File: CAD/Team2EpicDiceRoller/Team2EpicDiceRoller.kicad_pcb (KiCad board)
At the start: 2 copper layers, 45 parts, among them J1 Conn_02x03_Odd_Even, J2 Conn_01x16, J3 Conn_01x02_9VBatt, Q1 BS170, Q2 2N2222, SW3 RotaryEncoder_Switch, SW5 SW_LeftMenu, SW6 SW_MidMenu, SW7 SW_Reset, SW8 SW_RightMenu, U1 74HC14, U2 ATmega328P-P, Y1 Crystal_16MHz

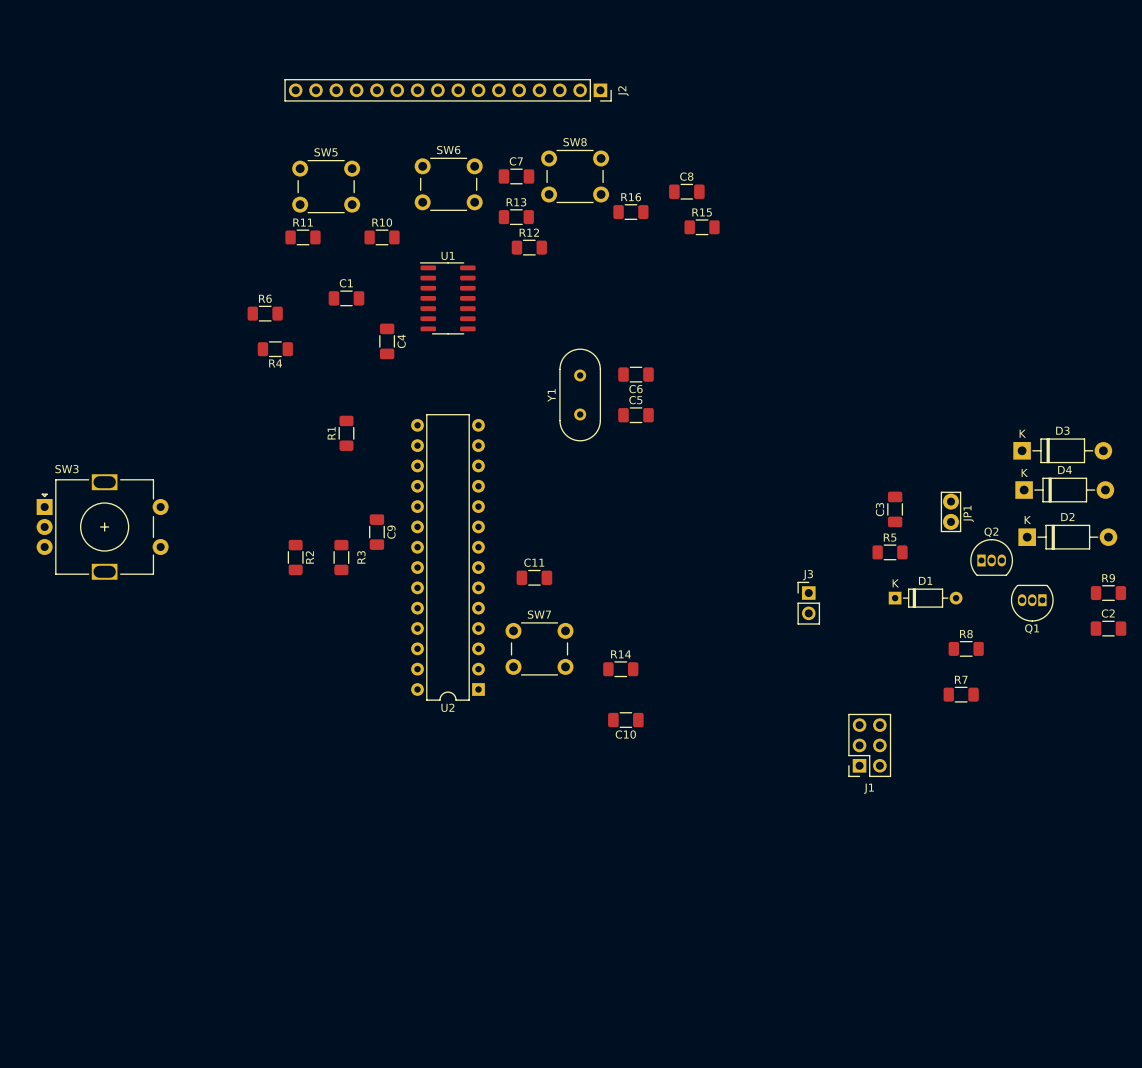
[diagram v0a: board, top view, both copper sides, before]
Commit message: Initial routing - done poorly, need to update power switch footprint
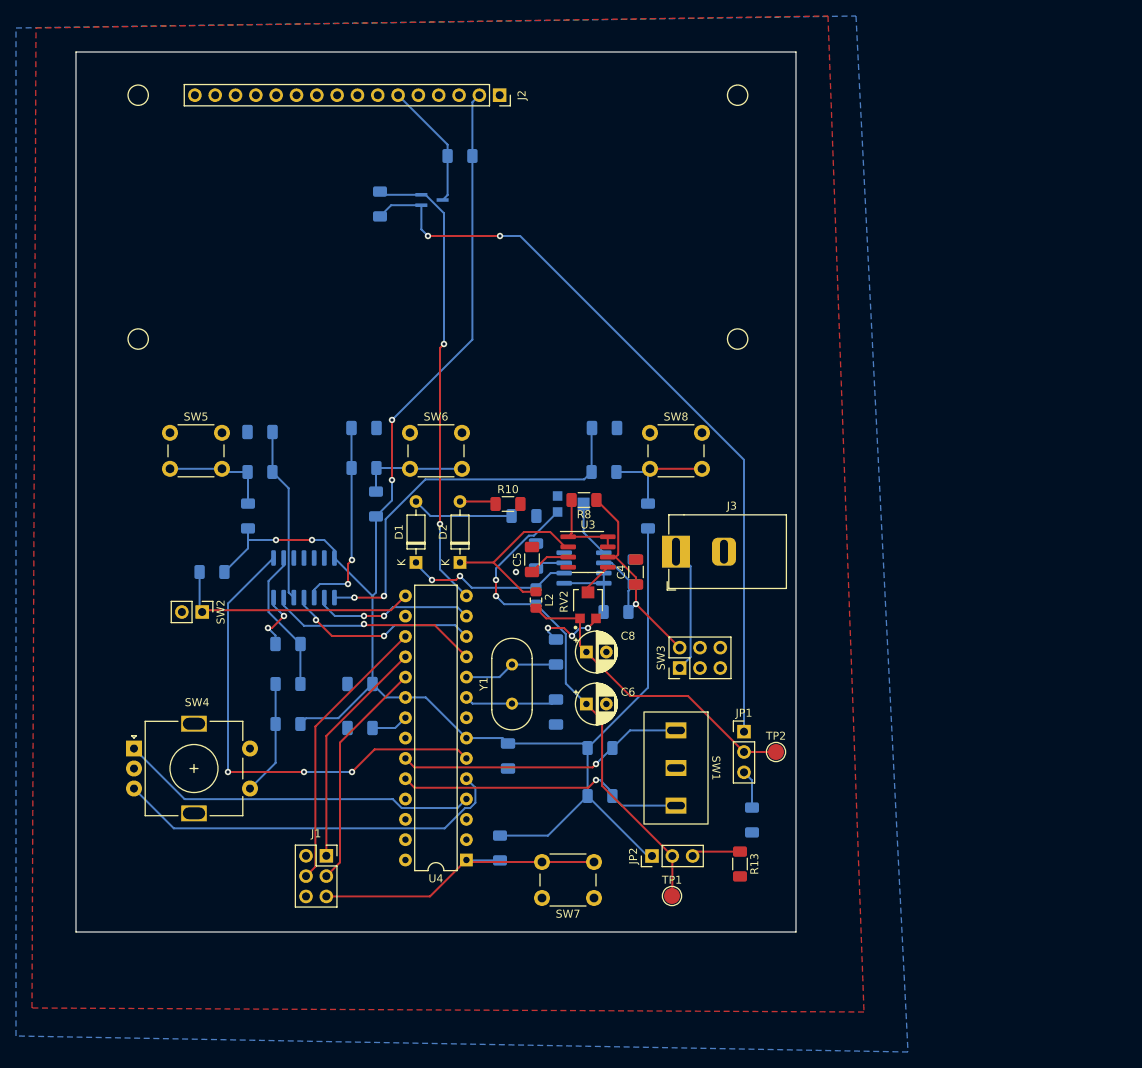
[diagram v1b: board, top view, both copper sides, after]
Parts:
- removed D3, D4: 1N4007, Diode_THT:D_DO-41_SOD81_P10.16mm_Horizontal
- removed Q2: 2N2222, Package_TO_SOT_THT:TO-92_Inline
- added C12: 10u, Capacitor_SMD:C_1206_3216Metric_Pad1.33x1.80mm_HandSolder, B.Cu at (163.1, 67.0)
- added C13: 100n, Capacitor_SMD:C_1206_3216Metric_Pad1.33x1.80mm_HandSolder, B.Cu at (132.5, 104.5)
- added C14: 100n, Capacitor_SMD:C_1206_3216Metric_Pad1.33x1.80mm_HandSolder, B.Cu at (151.0, 108.0)
- added C15: 100n, Capacitor_SMD:C_1206_3216Metric_Pad1.33x1.80mm_HandSolder, B.Cu at (132.5, 99.0)
- added JP2: Jumper_3_Open, Connector_PinHeader_2.54mm:PinHeader_1x03_P2.54mm_Vertical, F.Cu at (169.0, 120.5)
- added L1: 100u, Inductor_SMD:L_0805_2012Metric_Pad1.15x1.40mm_HandSolder, B.Cu at (154.5, 88.0)
- added L2: 100u, Inductor_SMD:L_0805_2012Metric_Pad1.15x1.40mm_HandSolder, F.Cu at (154.5, 88.5)
- added R17: 1k, Resistor_SMD:R_1206_3216Metric_Pad1.30x1.75mm_HandSolder, B.Cu at (133.0, 72.0)
- added R18: 10k, Resistor_SMD:R_1206_3216Metric_Pad1.30x1.75mm_HandSolder, B.Cu at (150.0, 119.5)
- added R19: 1k, Resistor_SMD:R_1206_3216Metric_Pad1.30x1.75mm_HandSolder, B.Cu at (168.5, 78.0)
- added R20: 1k, Resistor_SMD:R_1206_3216Metric_Pad1.30x1.75mm_HandSolder, B.Cu at (163.0, 72.5)
- added RV1: 5k, Library:TRIM_TC33X-2-502E, B.Cu at (159.0, 76.5)
- added RV2: 5k, Library:TRIM_TC33X-2-502E, F.Cu at (161.0, 89.0)
- added SW1: SW_Toggle_SPDT, Library:GoldSun_MTS103_Mini_Toggle_Switch, F.Cu at (172.0, 109.5)
- added SW2: Tilt_Switch, Connector_PinHeader_2.54mm:PinHeader_1x02_P2.54mm_Vertical, F.Cu at (112.8, 90.0)
- added SW4: RotaryEncoder_Switch, Rotary_Encoder:RotaryEncoder_Alps_EC11E-Switch_Vertical_H20mm, F.Cu at (104.2, 107.1)
- added TP1: TestPoint, TestPoint:TestPoint_Pad_D2.0mm, F.Cu at (171.5, 125.5)
- added TP2: TestPoint, TestPoint:TestPoint_Pad_D2.0mm, F.Cu at (184.5, 107.5)
- added U3: MC34063AD, Package_SO:SOIC-8_3.9x4.9mm_P1.27mm, F.Cu at (161.0, 82.5)
- added U4: ATmega328P-P, Package_DIP:DIP-28_W7.62mm, F.Cu at (145.8, 121.0)
- C1: value 10u -> 100u; moved to B.Cu
- C10, C9: value 100n -> 30p; moved to B.Cu
- C11: value 100n -> 10u; moved to B.Cu
- C2: value 1u -> 470p; moved to B.Cu
- C3: value 10p -> 10u; moved to B.Cu
- C4: value 10u -> 100u
- C5: value 30p -> 470p
- C6: value 30p -> 470u; footprint Capacitor_SMD:C_1206_3216Metric_Pad1.33x1.80mm_HandSolder -> Capacitor_THT:CP_Radial_D5.0mm_P2.50mm
- C7, R1, R11, R14, R15, R2, R3, R4, R6: moved to B.Cu
- C8: value 10u -> 470u; footprint Capacitor_SMD:C_1206_3216Metric_Pad1.33x1.80mm_HandSolder -> Capacitor_THT:CP_Radial_D5.0mm_P2.50mm
- D1: value BZX55C3V0 -> BZX55C5V1
- D2: value 1N4007 -> BZX55C3V9; footprint Diode_THT:D_DO-41_SOD81_P10.16mm_Horizontal -> Diode_THT:D_DO-35_SOD27_P7.62mm_Horizontal
- J3: value Conn_01x02_9VBatt -> Barrel_Jack; footprint Connector_PinHeader_2.54mm:PinHeader_1x02_P2.54mm_Vertical -> Library:BarrelJack_CUI_PJ-037A_Horizontal
- JP1: value Jumper_2_Bridged -> Jumper_3_Open; footprint TestPoint:TestPoint_Bridge_Pitch2.54mm_Drill1.0mm -> Connector_PinHeader_2.54mm:PinHeader_1x03_P2.54mm_Vertical
- Q1: value BS170 -> BSS138; footprint Package_TO_SOT_THT:TO-92_Inline -> Package_TO_SOT_SMD:SOT-323_SC-70_Handsoldering; moved to B.Cu
- R10: value 1k -> 120
- R12: value 1k -> 150; moved to B.Cu
- R13: value 1k -> 150
- R16: value 1k -> 10k; moved to B.Cu
- R5: value 2Meg -> 0.33; moved to B.Cu
- R7: value 2Meg -> 68; moved to B.Cu
- R8: value 500k -> 0.33
- R9: value 10K -> 1k; moved to B.Cu
- SW3: value RotaryEncoder_Switch -> SW_Power; footprint Rotary_Encoder:RotaryEncoder_Alps_EC11E-Switch_Vertical_H20mm -> Connector_PinHeader_2.54mm:PinHeader_2x03_P2.54mm_Vertical
- U1: value 74HC14 -> MC34063AD; footprint Package_SO:SOIC-14_3.9x8.7mm_P1.27mm -> Package_SO:SOIC-8_3.9x4.9mm_P1.27mm; moved to B.Cu
- U2: value ATmega328P-P -> 74HC14; footprint Package_DIP:DIP-28_W7.62mm -> Package_SO:SOIC-14_3.9x8.7mm_P1.27mm; moved to B.Cu
- moved R9 108.0 mm to (118.5, 78.0), turned to 90 degrees
- moved Q1 91.2 mm to (141.5, 38.5), turned to 0 degrees
- moved R13 85.6 mm to (180.0, 121.5), turned to -90 degrees
- moved SW3 81.9 mm to (172.5, 97.0), turned to 90 degrees
- moved C3 77.7 mm to (123.5, 94.0), turned to 180 degrees
- moved R12 76.8 mm to (181.5, 116.0), turned to -90 degrees
- moved C2 72.1 mm to (154.5, 83.0), turned to 90 degrees
- moved D2 71.0 mm to (145.0, 83.8), turned to 90 degrees
- moved J1 67.6 mm to (128.3, 120.5), turned to 0 degrees
- moved R14 65.5 mm to (135.0, 39.0), turned to 90 degrees
- moved D1 60.1 mm to (139.5, 83.8), turned to 90 degrees
- moved R7 59.0 mm to (153.0, 78.0)
- moved C8 58.9 mm to (160.8, 95.0)
- moved R15 53.5 mm to (134.5, 76.5), turned to 90 degrees
- moved R8 51.3 mm to (160.5, 76.0), turned to 180 degrees
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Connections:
- C1 pad 1: Net-(R6-Pad2) -> /Vin
- C10 pad 2: VCC -> Net-(C10-Pad2)
- C11 pad 1: GND -> /MidDebn
- C11 pad 2: VCC -> GND
- C2 pad 1: Net-(D4-Pad2) -> Net-(C2-Pad1)
- C3 pad 1: Net-(D2-Pad1) -> /EncDebnc
- C4 pad 1: Net-(R11-Pad2) -> /Vin
- C5 pad 1: GND -> Net-(C5-Pad1)
- C5 pad 2: Net-(U2-Pad9) -> GND
- C6 pad 1: GND -> Net-(C6-Pad1)
- C6 pad 2: Net-(U2-Pad10) -> GND
- C7 pad 1: Net-(R13-Pad2) -> /LeftDebn
- C8 pad 1: Net-(R16-Pad2) -> Net-(C8-Pad1)
- J1 pad 2: ICSP_5V -> unconnected-(J1-Pad2)
- J2 pad 6: IO8_PB0 -> LCD_RX
- JP1 pad 1: Net-(D2-Pad1) -> +3V3
- Q1 pad 1: Net-(D2-Pad2) -> +3V3
- Q1 pad 2: Net-(Q1-Pad2) -> IO8_PB0
- Q1 pad 3: Net-(D1-Pad2) -> LCD_RX
- R10 pad 1: VCC -> Net-(D2-Pad2)
- R10 pad 2: Net-(R10-Pad2) -> GND
- R11 pad 1: Net-(R10-Pad2) -> Net-(R11-Pad1)
- R11 pad 2: Net-(R11-Pad2) -> /LeftDebn
- R12 pad 1: VCC -> Net-(JP1-Pad3)
- R12 pad 2: Net-(R12-Pad2) -> GND
- R13 pad 1: Net-(R12-Pad2) -> Net-(JP2-Pad3)
- R13 pad 2: Net-(R13-Pad2) -> GND
- R14 pad 1: VCC -> +3V3
- R14 pad 2: RESET# -> IO8_PB0
- R16 pad 1: Net-(R15-Pad2) -> VCC
- R16 pad 2: Net-(R16-Pad2) -> LCD_RX
- R5 pad 1: Net-(D1-Pad1) -> /Vin
- R5 pad 2: Net-(Q1-Pad2) -> Net-(R5-Pad2)
- R6 pad 2: Net-(R6-Pad2) -> /EncDebnc
- R7 pad 1: ICSP_5V -> Net-(D1-Pad2)
- R7 pad 2: Net-(Q2-Pad2) -> GND
- R8 pad 1: Net-(Q2-Pad2) -> /Vin
- R8 pad 2: GND -> Net-(R8-Pad2)
- R9 pad 1: Net-(D2-Pad1) -> VCC
- R9 pad 2: Net-(D4-Pad2) -> Net-(R11-Pad1)
- SW5 pad 2: Net-(R10-Pad2) -> Net-(R11-Pad1)
- SW6 pad 2: Net-(R12-Pad2) -> Net-(R15-Pad2)
- SW8 pad 2: Net-(R15-Pad2) -> Net-(R19-Pad2)
- U1 pad 1: Net-(R6-Pad2) -> Net-(R5-Pad2)
- U1 pad 2: IO4_PD4 -> Net-(D1-Pad1)
- U1 pad 3: Net-(R11-Pad2) -> Net-(C2-Pad1)
- U1 pad 4: IO5_PD5 -> GND
- U1 pad 5: Net-(R13-Pad2) -> Net-(RV1-Pad2)
- U1 pad 6: IO6_PD6 -> /Vin
- U1 pad 7: GND -> Net-(R5-Pad2)
- U1 pad 8: IO7_PD7 -> Net-(R5-Pad2)
- U2 pad 1: RESET# -> /RigDebn
- U2 pad 10: Net-(U2-Pad10) -> unconnected-(U2-Pad10)
- U2 pad 11: IO5_PD5 -> GND
- U2 pad 12: IO6_PD6 -> unconnected-(U2-Pad12)
- U2 pad 13: IO7_PD7 -> GND
- U2 pad 14: IO8_PB0 -> VCC
- U2 pad 2: IO0_RX_PD0 -> IO7_PD7
- U2 pad 3: IO1_TX_PD1 -> /MidDebn
- U2 pad 4: IO2_PD2 -> IO6_PD6
- U2 pad 5: IO3_PD3 -> /LeftDebn
- U2 pad 6: IO4_PD4 -> IO5_PD5
- U2 pad 7: VCC -> GND
- U2 pad 8: GND -> IO4_PD4
- U2 pad 9: Net-(U2-Pad9) -> /EncDebnc
- Y1 pad 1: Net-(U2-Pad9) -> Net-(C9-Pad2)
- Y1 pad 2: Net-(U2-Pad10) -> Net-(C10-Pad2)
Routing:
- net VCC: track 0.00 -> 206.9 mm, vias 0 -> 4
- net +3V3: track 0.00 -> 95.0 mm, vias 0 -> 2
- net Net-(C6-Pad1): track 0.00 -> 63.0 mm, vias 0 -> 2
- net IO4_PD4: track 0.00 -> 60.5 mm, vias 0 -> 3
- net IO8_PB0: track 0.00 -> 58.5 mm, vias 0 -> 2
- net /RigDebn: track 0.00 -> 49.7 mm, vias 0 -> 2
- net IO3_PD3: track 0.00 -> 49.5 mm
- net IO2_PD2: track 0.00 -> 45.1 mm
- net RESET#: track 0.00 -> 39.7 mm
- net Net-(C8-Pad1): track 0.00 -> 39.4 mm
- net AD1_PC1: track 0.00 -> 36.3 mm, vias 0 -> 1
- net AD0_PC0: track 0.00 -> 36.2 mm, vias 0 -> 1
- net IO11_MOSI_PB3: track 0.00 -> 35.1 mm
- net /Vin: track 0.00 -> 34.2 mm, vias 0 -> 1
- net IO9_PB1: track 0.00 -> 31.4 mm
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- added copper zone on B.Cu, net GND
- added copper zone on F.Cu, net GND
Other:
- board outline added: 90 x 110 mm

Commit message: Updated schematic to remove traces and update the footprints
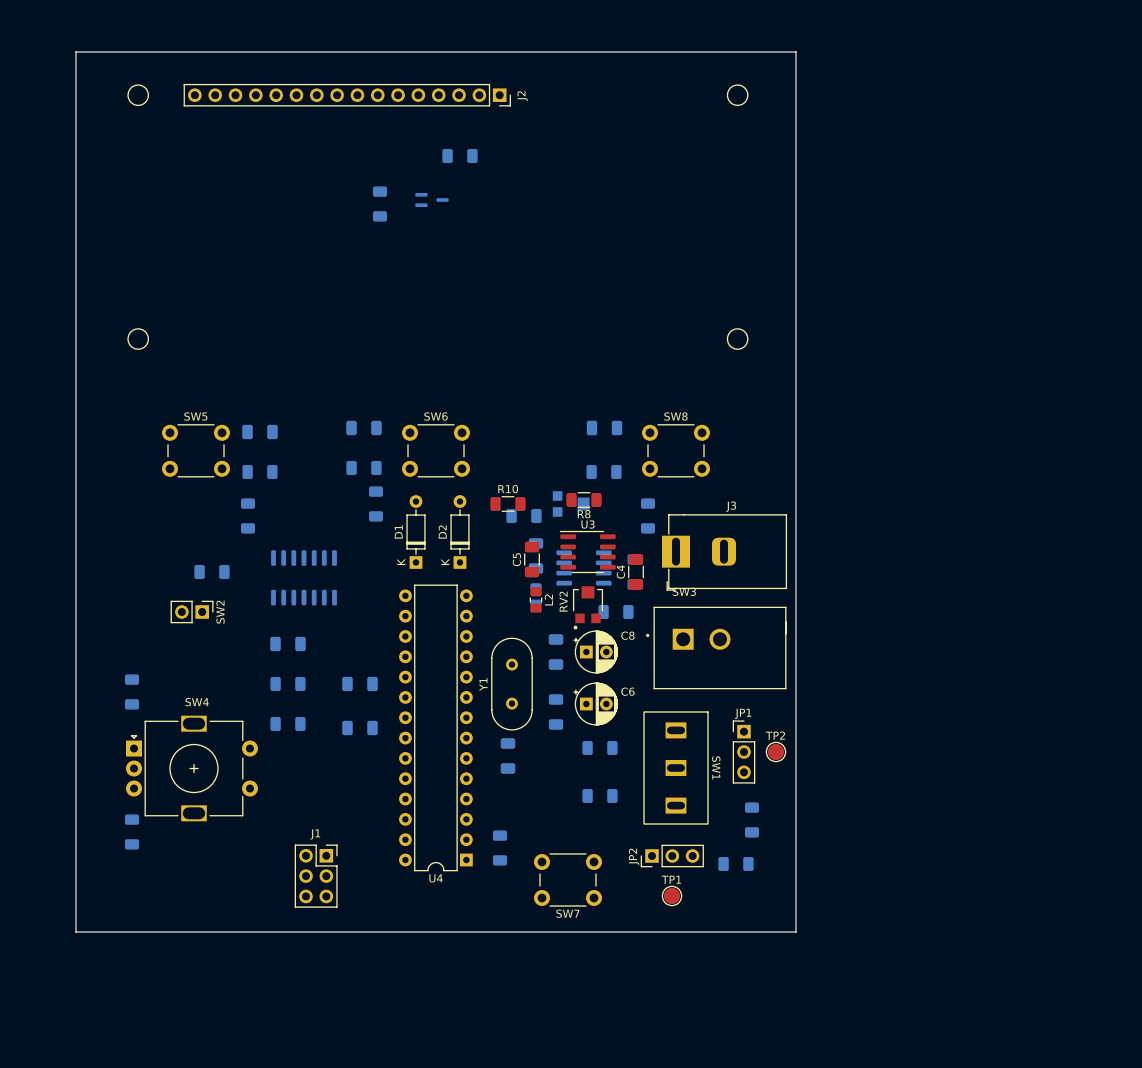
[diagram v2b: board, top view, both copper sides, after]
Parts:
- added R21: 5.1k, Resistor_SMD:R_1206_3216Metric_Pad1.30x1.75mm_HandSolder, B.Cu at (104.0, 100.0)
- added R22: 5.1k, Resistor_SMD:R_1206_3216Metric_Pad1.30x1.75mm_HandSolder, B.Cu at (104.0, 117.5)
- R13: moved to B.Cu
- SW3: footprint Connector_PinHeader_2.54mm:PinHeader_2x03_P2.54mm_Vertical -> GF-123-0054:SW_GF-123-0054
- moved SW3 5.63 mm to (177.5, 94.5), turned to 0 degrees
- moved R13 0.50 mm to (179.5, 121.5), turned to 0 degrees
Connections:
- SW4 pad A: IO2_PD2 -> Net-(R21-Pad1)
- SW4 pad B: IO3_PD3 -> Net-(R22-Pad2)
- SW4 pad MP: (no net) -> GND
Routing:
- net VCC: track 206.9 -> 0.00 mm, vias 4 -> 0
- net +3V3: track 95.0 -> 0.00 mm, vias 2 -> 0
- net Net-(C6-Pad1): track 63.0 -> 0.00 mm, vias 2 -> 0
- net IO4_PD4: track 60.5 -> 0.00 mm, vias 3 -> 0
- net IO8_PB0: track 58.5 -> 0.00 mm, vias 2 -> 0
- net /RigDebn: track 49.7 -> 0.00 mm, vias 2 -> 0
- net IO3_PD3: track 49.5 -> 0.00 mm
- net IO2_PD2: track 45.1 -> 0.00 mm
- net RESET#: track 39.7 -> 0.00 mm
- net Net-(C8-Pad1): track 39.4 -> 0.00 mm
- net AD1_PC1: track 36.3 -> 0.00 mm, vias 1 -> 0
- net AD0_PC0: track 36.2 -> 0.00 mm, vias 1 -> 0
- net IO11_MOSI_PB3: track 35.1 -> 0.00 mm
- net /Vin: track 34.2 -> 0.00 mm, vias 1 -> 0
- net IO9_PB1: track 31.4 -> 0.00 mm
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- removed copper zone on B.Cu, net GND
- removed copper zone on F.Cu, net GND

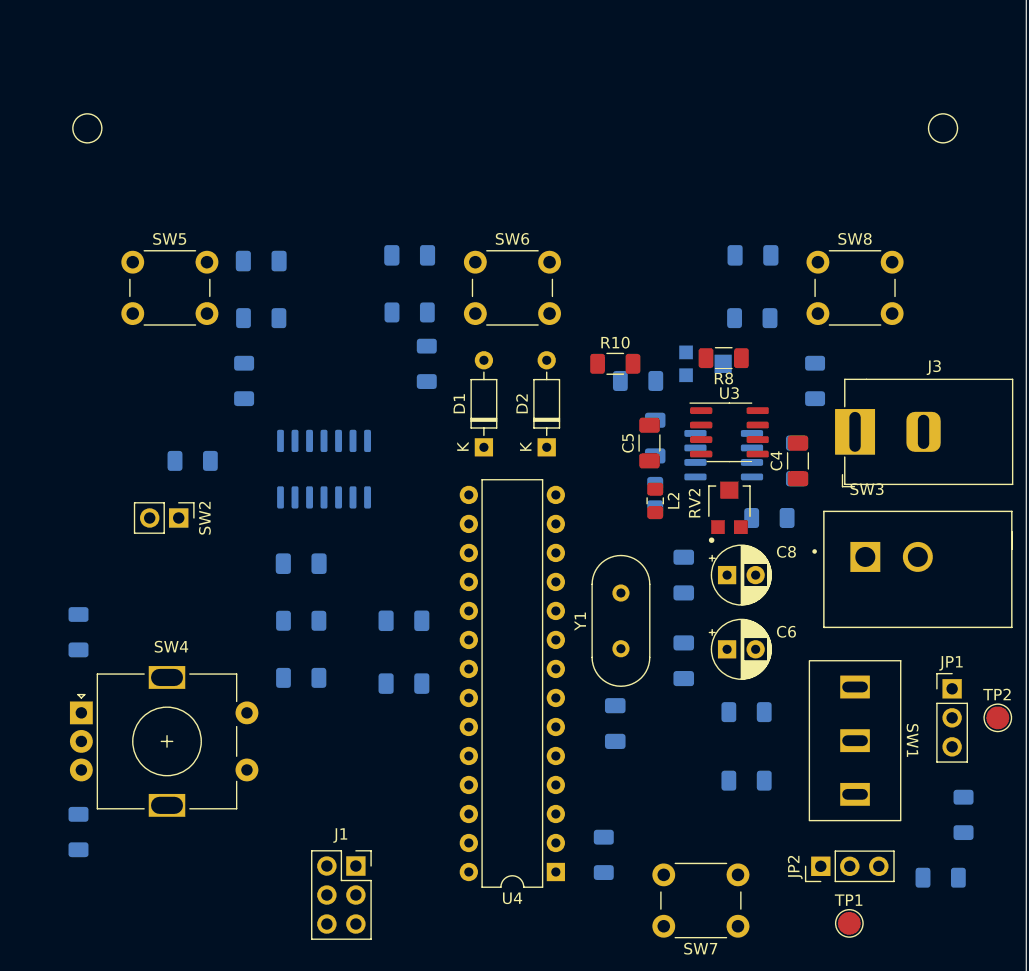
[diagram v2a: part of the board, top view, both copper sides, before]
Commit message: Added mounting holes for the standoffs
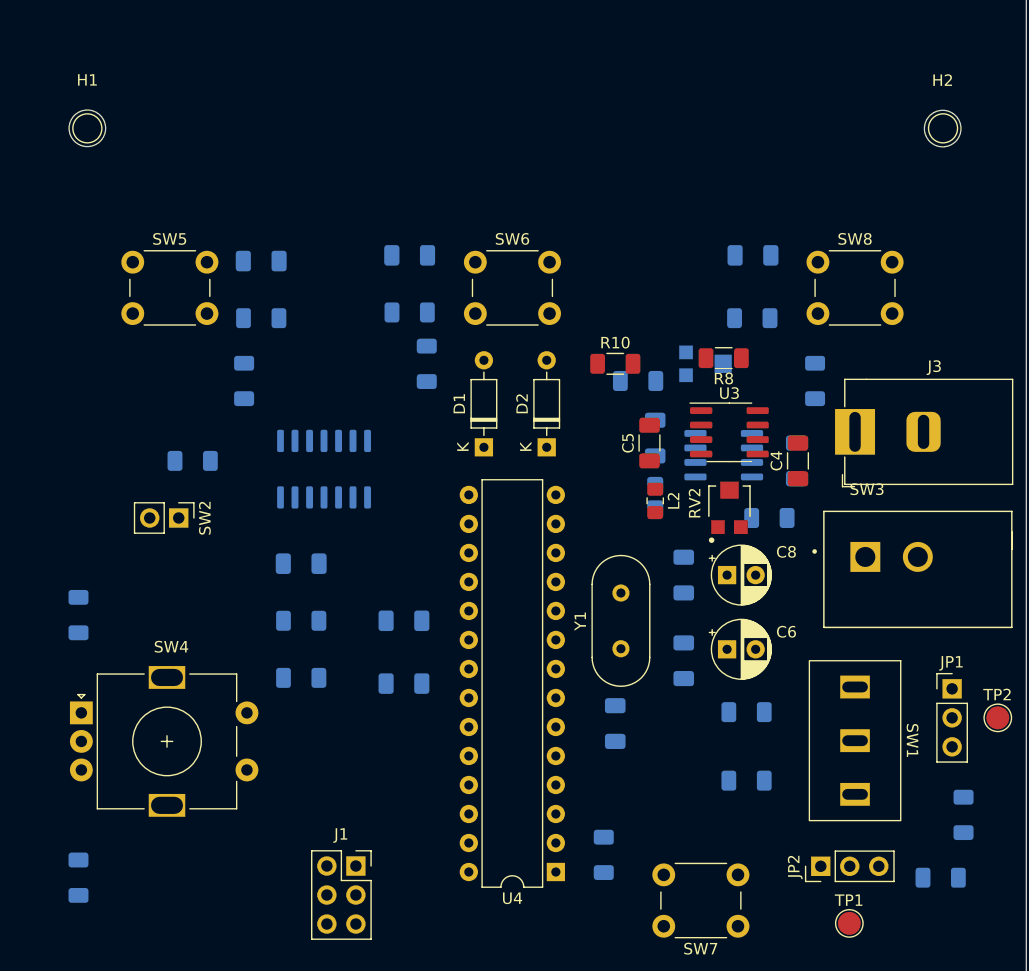
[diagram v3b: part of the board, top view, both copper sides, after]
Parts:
- added H1: MountingHole, MountingHole:MountingHole_3.2mm_M3, F.Cu at (104.8, 55.9)
- added H2: MountingHole, MountingHole:MountingHole_3.2mm_M3, F.Cu at (179.7, 55.9)
- J2: footprint Connector_PinSocket_2.54mm:PinSocket_1x16_P2.54mm_Vertical -> Library:PinSocket_1x16_P2.54mm_Vertical_LCD
- moved R22 4.00 mm to (104.0, 121.5)
- moved R21 1.50 mm to (104.0, 98.5)
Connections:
- net Net-(JP1-Pad3) renamed /Load_3V3
- net Net-(JP2-Pad3) renamed /Load_VCC
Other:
- rule pad_to_mask_clearance: 0 -> 0.0508

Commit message: Newer version
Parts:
- added TPG1: TestPointGND, TestPoint:TestPoint_Pad_D2.0mm, F.Cu at (168.7, 88.0)
- added TPG2: TestPointGND, TestPoint:TestPoint_Pad_D2.0mm, F.Cu at (101.1, 95.3)
- C1, C2, L1, R13, R5, R7, RV1, U1: moved to F.Cu
- TP1: value TestPoint -> TestPointVCC
- TP2: value TestPoint -> TestPoint3V3
- moved TP2 85.0 mm to (101.1, 90.7)
- moved R12 78.5 mm to (104.7, 99.6)
- moved JP1 77.6 mm to (104.8, 88.0)
- moved SW4 62.8 mm to (166.8, 113.2)
- moved R2 61.3 mm to (101.7, 120.8)
- moved R3 61.2 mm to (101.5, 111.5)
- moved SW1 60.7 mm to (111.6, 115.7)
- moved L2 59.7 mm to (110.2, 48.4)
- moved R21 57.2 mm to (159.8, 110.9), turned to 180 degrees
- moved R22 56.1 mm to (159.8, 116.0), turned to 0 degrees
- moved D2 54.9 mm to (112.0, 40.0), turned to 0 degrees
- moved U3 52.7 mm to (123.2, 45.8)
- moved C5 51.9 mm to (115.8, 48.4)
- moved C8 49.8 mm to (111.2, 90.0), turned to -90 degrees
- moved RV2 48.9 mm to (112.4, 83.8)
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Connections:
- net Net-(C8-Pad1) renamed /3V3
- C6 pad 1: Net-(C6-Pad1) -> VCC
- JP2 pad 2: Net-(C6-Pad1) -> VCC
- L1 pad 2: Net-(C6-Pad1) -> VCC
- RV1 pad 1: Net-(C6-Pad1) -> VCC
- TP1 pad 1: Net-(C6-Pad1) -> VCC
- U2 pad 1: /RigDebn -> /LeftDebn
- U2 pad 2: IO7_PD7 -> IO5_PD5
- U2 pad 5: /LeftDebn -> /RigDebn
- U2 pad 6: IO5_PD5 -> IO7_PD7
